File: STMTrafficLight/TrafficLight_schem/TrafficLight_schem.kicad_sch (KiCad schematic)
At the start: 4 parts, among them P1 Conn_01x25, P2 Conn_01x25, P3 Conn_01x25, P4 Conn_01x25

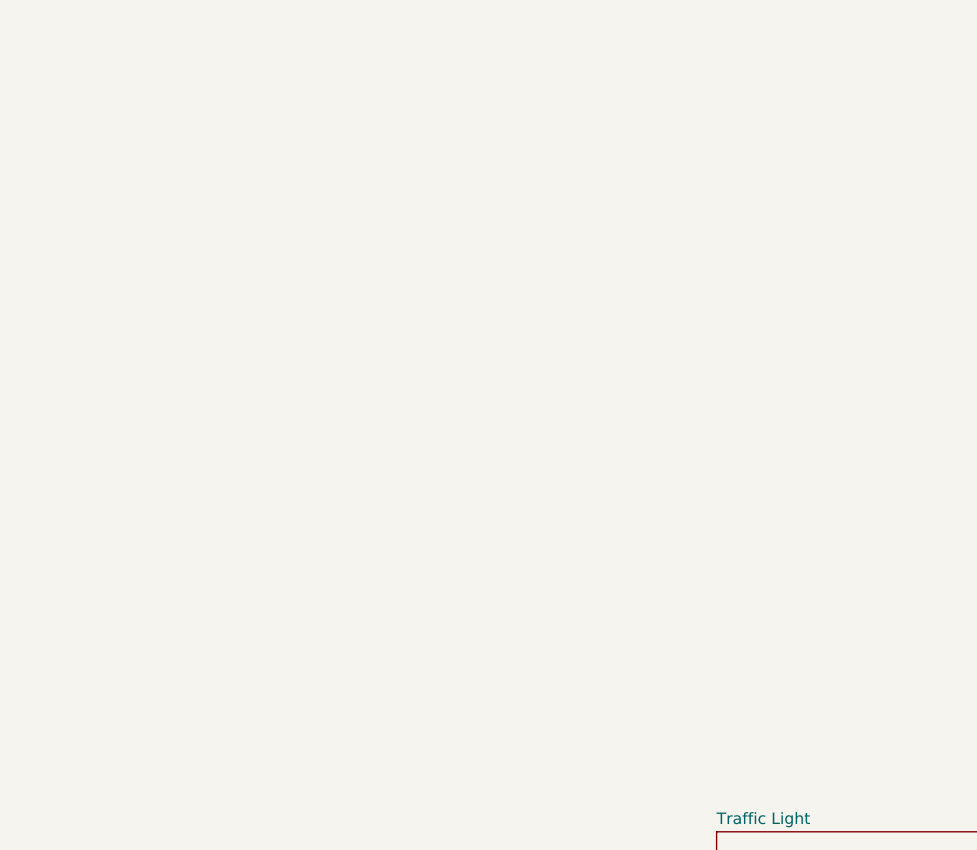
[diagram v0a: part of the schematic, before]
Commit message: continued on the traffic light shield
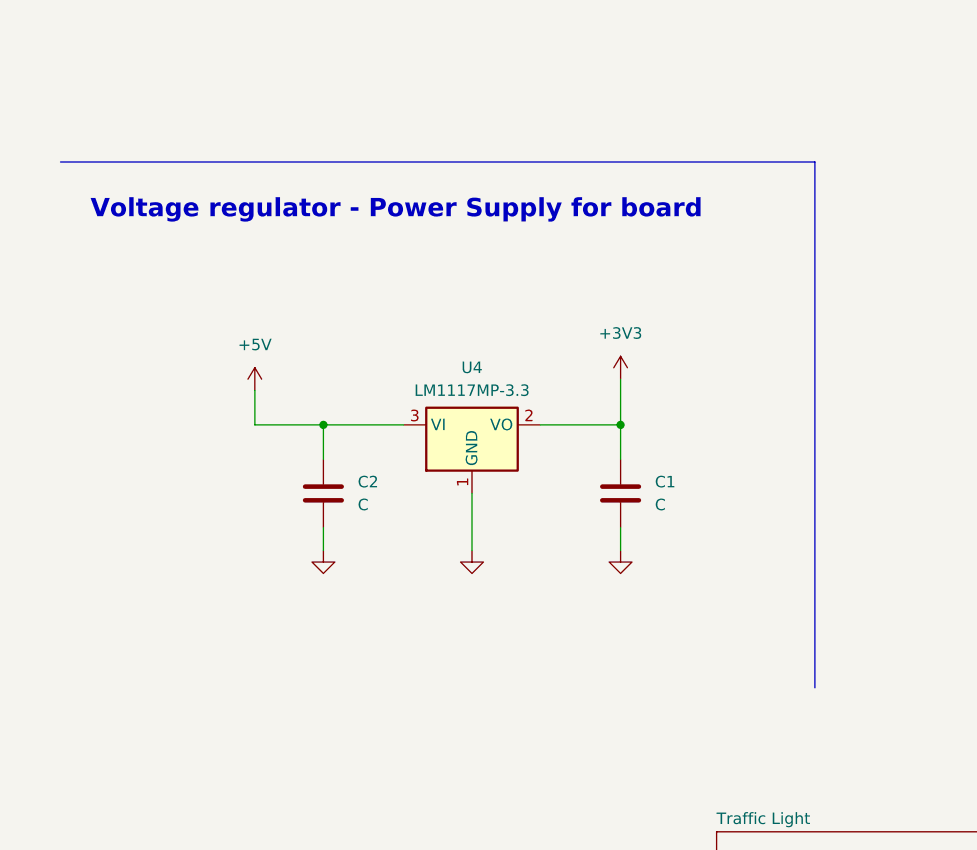
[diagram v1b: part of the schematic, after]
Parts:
- added C1, C2: C, symbol Device:C
- added U4: LM1117MP-3.3, Package_TO_SOT_SMD:SOT-223-3_TabPin2, symbol Regulator_Linear:LM1117MP-3.3
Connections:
- new net +3V3: C1.1, U4.2 (VO)
- new net +5V: C2.1, U4.3 (VI)
- new net GND: C1.2, C2.2, U4.1 (GND)
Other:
- note added: "Voltage regulator - Power Supply for board"
